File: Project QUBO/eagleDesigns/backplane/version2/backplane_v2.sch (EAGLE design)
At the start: 23 parts, among them U1 TUSB2077ALQFP

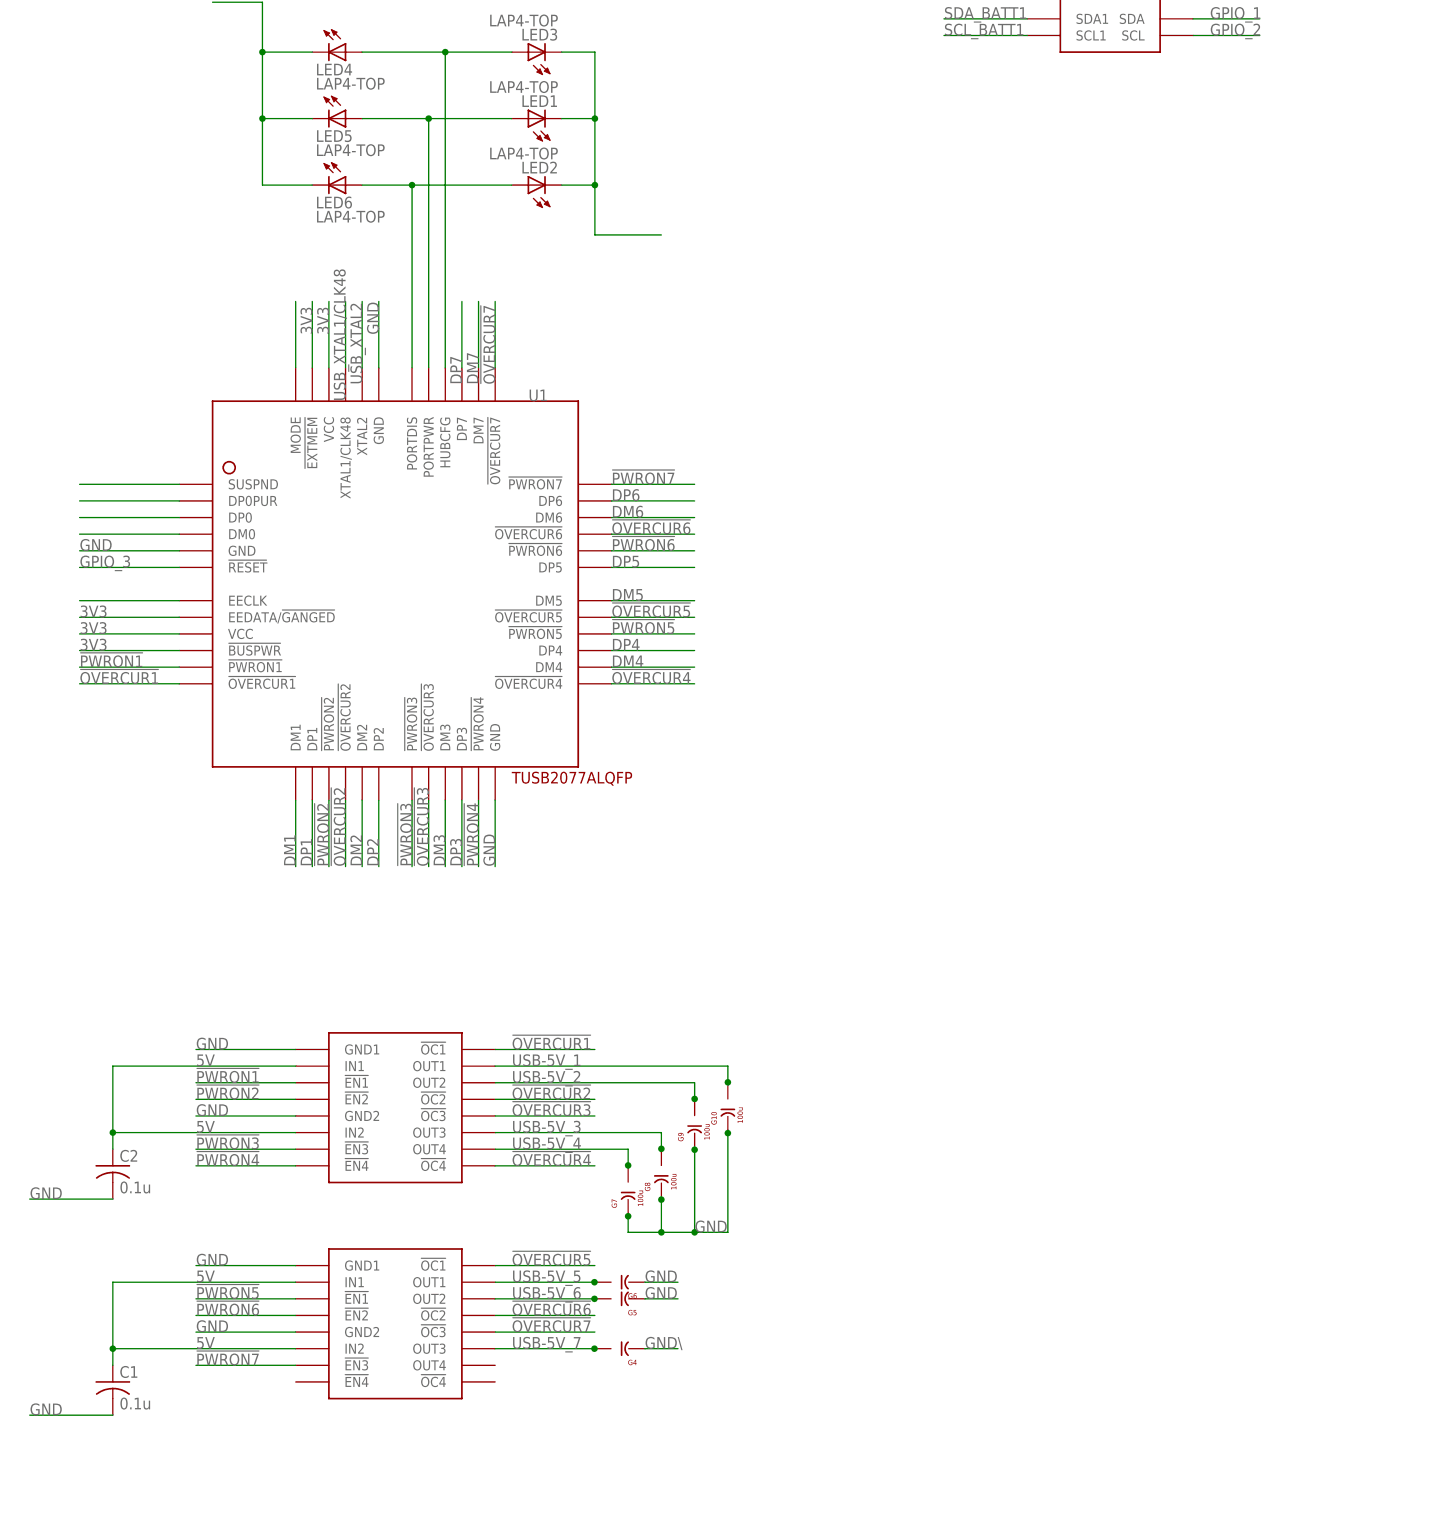
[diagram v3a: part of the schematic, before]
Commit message: 
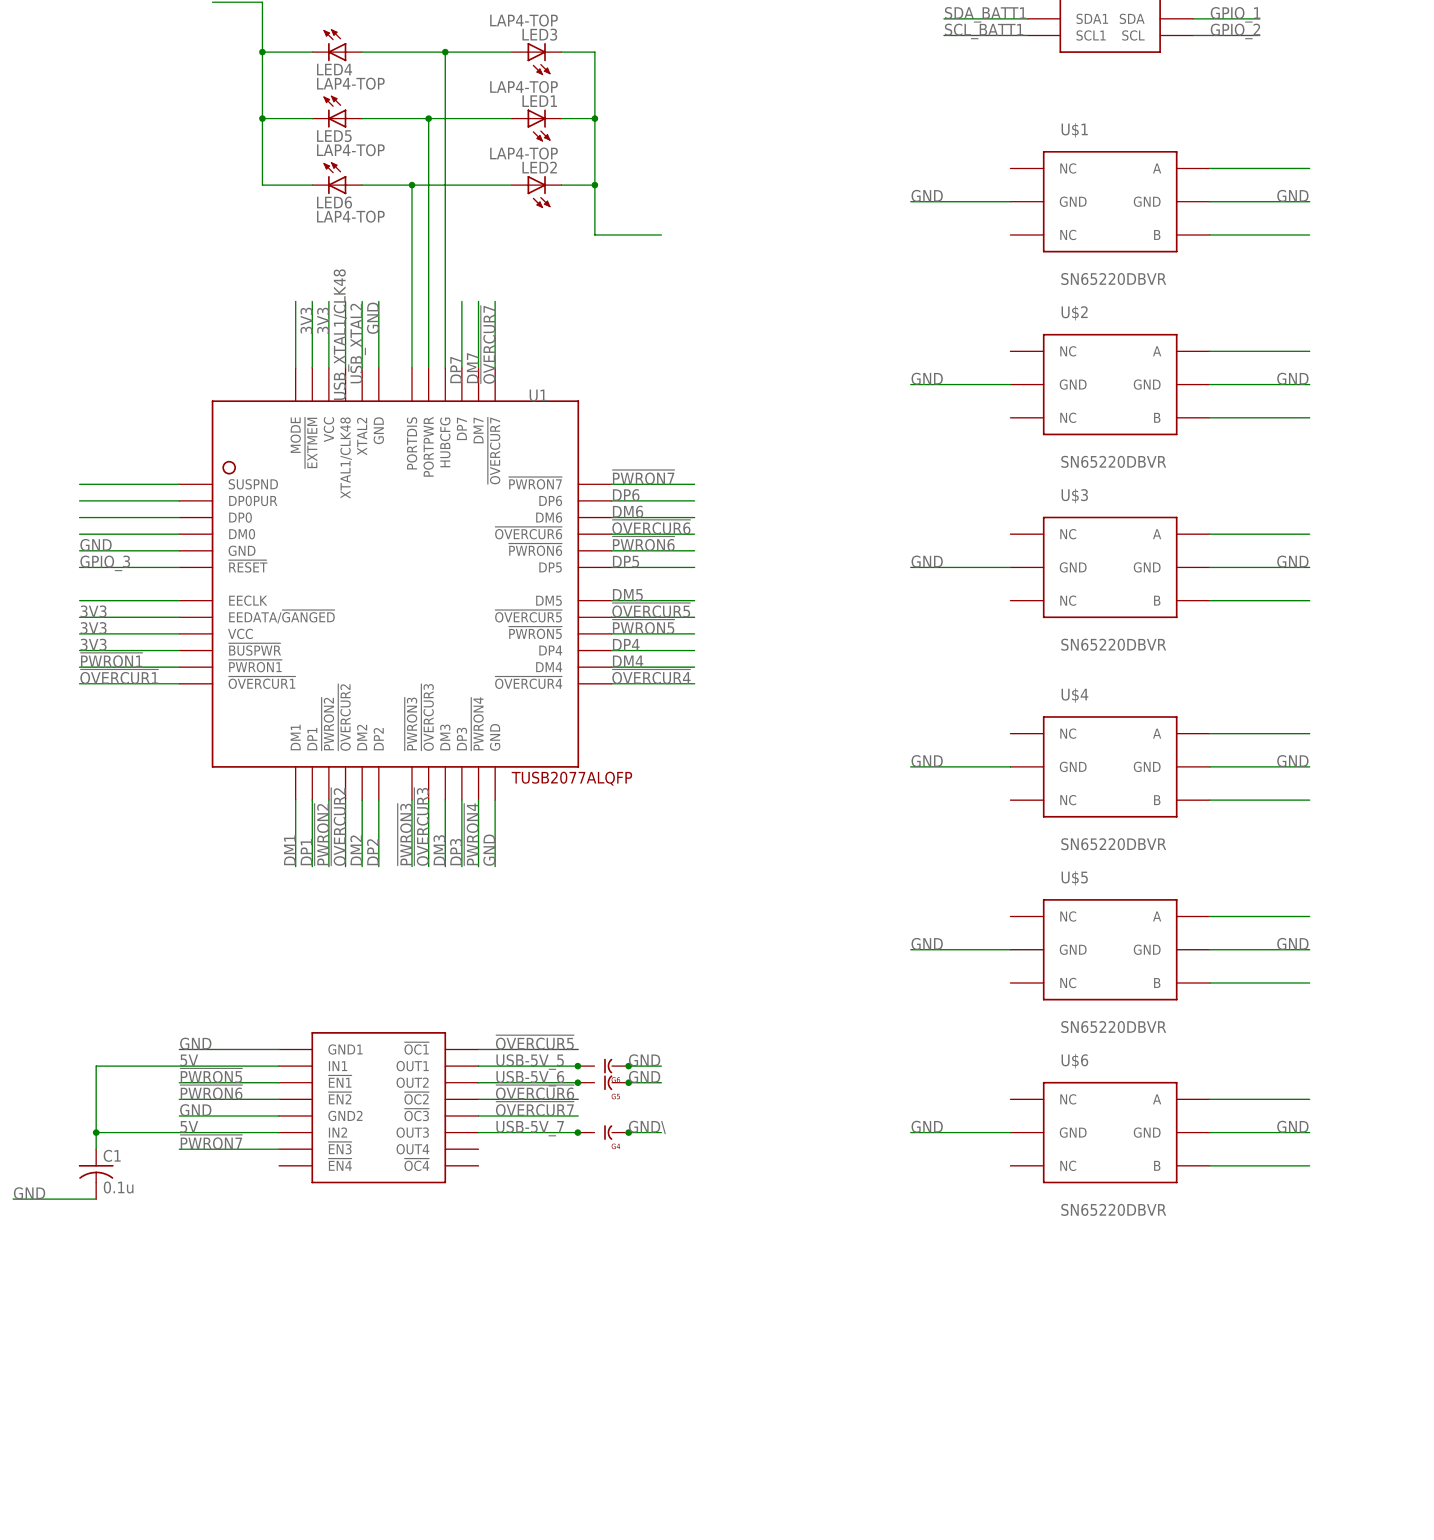
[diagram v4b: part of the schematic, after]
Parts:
- removed C2: 0.1u, resistor:C-USC0603
- removed G10, G7, G8, G9: 100u, avx:F930J107MBA
- removed G2: (no value), texas:TPS2044BBD-SOIC
- added U$1, U$2, U$3, U$4, U$5, U$6: SN65220DBVR, texas:SN65220DBVR
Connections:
- removed net USB-5V_1: G10.+, G2.OUT1
- removed net USB-5V_2: G2.OUT2, G9.+
- removed net USB-5V_3: G2.OUT3, G8.+
- removed net USB-5V_4: G2.OUT4, G7.+
- new net GND\: G4.-
- new net N$10: U$1.B
- new net N$11: U$3.A
- new net N$12: U$3.B
- new net N$13: U$4.A
- new net N$14: U$4.B
- new net N$15: U$5.A
- new net N$16: U$5.B
- new net N$17: U$6.A
- new net N$18: U$6.B
- new net N$6: U$2.A
- new net N$8: U$2.B
- new net N$9: U$1.A
- net !OVERCUR1!: no longer G2.!OC1!
- net !OVERCUR2!: no longer G2.!OC2!
- net !OVERCUR3!: no longer G2.!OC3!
- net !OVERCUR4!: no longer G2.!OC4!
- net !PWRON1!: no longer G2.!EN1!
- net !PWRON2!: no longer G2.!EN2!
- net !PWRON3!: no longer G2.!EN3!
- net !PWRON4!: no longer G2.!EN4!
- net 5V: no longer C2.1, G2.IN1, G2.IN2
- net GND: now also G5.-, G6.-, U$1.GND@2, U$1.GND@5, U$2.GND@2, U$2.GND@5, U$3.GND@2, U$3.GND@5, U$4.GND@2, U$4.GND@5, U$5.GND@2, U$5.GND@5, U$6.GND@2, U$6.GND@5; no longer C2.2, G10.-, G2.GND1, G2.GND2, G7.-, G8.-, G9.-
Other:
- moved on the sheet: C1, G4, G5, G6

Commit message: 
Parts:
- removed G4, G5, G6: (no value), avx:F930J107MBA
- removed JP2, JP3, JP4: MPTC-01-80, samtec:MPTC-01-80
- removed LED1, LED2, LED3, LED4, LED5, LED6: LAP4-TOP, led:LAP4-TOP
- added C2, C3: (no value), resistor:C-USC0805
- added CPU_USB_CPU: (no value), molex:KK254_VERT_2PIN22-29-2021
- added CPU_USB_CPU_TRANS, U$7: SN65220DBVR, texas:SN65220DBVR
- added R1, R2: 27, resistor:R-US_R0805
- added R3: 1.5k, resistor:R-US_R0805
- renumbered G3 to 7USB_PWR, U1 to 7USB
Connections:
- removed net GPIO_10: JP1.P$12, JP2.P$12, JP3.P$12, JP4.P$12
- removed net GPIO_11: JP1.P$13, JP2.P$13, JP3.P$13, JP4.P$13
- removed net GPIO_12: JP1.P$14, JP2.P$14, JP3.P$14, JP4.P$14
- removed net GPIO_13: JP1.P$15, JP2.P$15, JP3.P$15, JP4.P$15
- removed net GPIO_14: JP1.P$16, JP2.P$16, JP3.P$16, JP4.P$16
- removed net GPIO_15: JP1.P$23, JP2.P$23, JP3.P$23, JP4.P$23
- removed net GPIO_16: JP1.P$24, JP2.P$24, JP3.P$24, JP4.P$24
- removed net GPIO_17: JP1.P$25, JP2.P$25, JP3.P$25, JP4.P$25
- removed net GPIO_18: JP1.P$26, JP2.P$26, JP3.P$26, JP4.P$26
- removed net GPIO_19: JP1.P$27, JP2.P$27, JP3.P$27, JP4.P$27
- removed net GPIO_20: JP1.P$28, JP2.P$28, JP3.P$28, JP4.P$28
- removed net GPIO_21: JP1.P$29, JP2.P$29, JP3.P$29, JP4.P$29
- removed net GPIO_22: JP1.P$30, JP2.P$30, JP3.P$30, JP4.P$30
- removed net GPIO_23: JP1.P$31, JP2.P$31, JP3.P$31, JP4.P$31
- removed net GPIO_24: JP1.P$32, JP2.P$32, JP3.P$32, JP4.P$32
- removed net GPIO_25: JP1.P$33, JP2.P$33, JP3.P$33, JP4.P$33
- removed net GPIO_26: JP1.P$34, JP2.P$34, JP3.P$34, JP4.P$34
- removed net GPIO_27: JP1.P$35, JP2.P$35, JP3.P$35, JP4.P$35
- removed net GPIO_28: JP1.P$36, JP2.P$36, JP3.P$36, JP4.P$36
- removed net GPIO_29: JP1.P$43, JP2.P$43, JP3.P$43, JP4.P$43
- removed net GPIO_30: JP1.P$44, JP2.P$44, JP3.P$44, JP4.P$44
- removed net GPIO_31: JP1.P$45, JP2.P$45, JP3.P$45, JP4.P$45
- removed net GPIO_32: JP1.P$46, JP2.P$46, JP3.P$46, JP4.P$46
- removed net GPIO_33: JP1.P$47, JP2.P$47, JP3.P$47, JP4.P$47
- removed net GPIO_34: JP1.P$48, JP2.P$48, JP3.P$48, JP4.P$48
- removed net GPIO_35: JP1.P$49, JP2.P$49, JP3.P$49, JP4.P$49
- removed net GPIO_36: JP1.P$50, JP2.P$50, JP3.P$50, JP4.P$50
- removed net GPIO_37: JP1.P$51, JP2.P$51, JP3.P$51, JP4.P$51
- removed net GPIO_38: JP1.P$52, JP2.P$52, JP3.P$52, JP4.P$52
- removed net GPIO_39: JP1.P$53, JP2.P$53, JP3.P$53, JP4.P$53
- removed net GPIO_40: JP1.P$54, JP2.P$54, JP3.P$54, JP4.P$54
- removed net GPIO_41: JP1.P$55, JP2.P$55, JP3.P$55, JP4.P$55
- removed net GPIO_42: JP1.P$56, JP2.P$56, JP3.P$56, JP4.P$56
- removed net GPIO_43: JP1.P$63, JP2.P$63, JP3.P$63, JP4.P$63
- removed net GPIO_44: JP1.P$64, JP2.P$64, JP3.P$64, JP4.P$64
- removed net GPIO_45: JP1.P$65, JP2.P$65, JP3.P$65, JP4.P$65
- removed net GPIO_46: JP1.P$66, JP2.P$66, JP3.P$66, JP4.P$66
- removed net GPIO_47: JP1.P$67, JP2.P$67, JP3.P$67, JP4.P$67
- removed net GPIO_48: JP1.P$68, JP2.P$68, JP3.P$68, JP4.P$68
- removed net GPIO_49: JP1.P$69, JP2.P$69, JP3.P$69, JP4.P$69
- removed net GPIO_50: JP1.P$70, JP2.P$70, JP3.P$70, JP4.P$70
- removed net GPIO_51: JP1.P$71, JP2.P$71, JP3.P$71, JP4.P$71
- removed net GPIO_52: JP1.P$72, JP2.P$72, JP3.P$72, JP4.P$72
- removed net GPIO_53: JP1.P$73, JP2.P$73, JP3.P$73, JP4.P$73
- removed net GPIO_54: JP1.P$74, JP2.P$74, JP3.P$74, JP4.P$74
- removed net GPIO_55: JP1.P$75, JP2.P$75, JP3.P$75, JP4.P$75
- removed net GPIO_56: JP1.P$76, JP2.P$76, JP3.P$76, JP4.P$76
- removed net GPIO_9: JP1.P$11, JP2.P$11, JP3.P$11, JP4.P$11
- removed net N$3: 7USB.DP0
- removed net N$4: 7USB.DM0
- removed net N$43: 7USB.PORTDIS, LED2.A, LED6.A
- removed net N$44: 7USB.PORTPWR, LED1.A, LED5.A
- removed net N$45: 7USB.HUBCFG, LED3.A, LED4.A
- removed net THR_SCL: JP1.P$1, JP2.P$1, JP3.P$1, JP4.P$1
- removed net THR_SDA: JP1.P$2, JP2.P$2, JP3.P$2, JP4.P$2
- removed net USB-M_1: JP1.P$61
- removed net USB-M_2: JP2.P$61
- removed net USB-M_3: JP3.P$61
- removed net USB-M_4: JP4.P$61
- removed net USB-P_1: JP1.P$41
- removed net USB-P_2: JP2.P$41
- removed net USB-P_3: JP3.P$41
- removed net USB-P_4: JP4.P$41
- new net CANH: JP1.P$25
- new net CANL: JP1.P$26
- new net CE_0: JP1.P$52
- new net CE_1: JP1.P$53
- new net CE_2: JP1.P$54
- new net CE_3: JP1.P$55
- new net CE_4: JP1.P$56
- new net CPU_USB_CPU_D+: 7USB.DP0, C3.1, CPU_USB_CPU_TRANS.A, R1.2, R3.1
- new net CPU_USB_CPU_D-: 7USB.DM0, C2.1, CPU_USB_CPU_TRANS.B, R2.2
- new net CTS_0: JP1.P$47
- new net CTS_1: JP1.P$31
- new net CTS_2: JP1.P$71
- new net CTS_3: JP1.P$75
- new net CTS_4: JP1.P$79
- new net FLEX_USB_1+\: JP1.P$17
- new net FLEX_USB_1-: JP1.P$16
- new net FLEX_USB_2+: JP1.P$14
- new net FLEX_USB_2-: JP1.P$13
- new net GPIO_0: JP1.P$35
- new net MISO: JP1.P$51
- new net MOSI: JP1.P$50
- new net N$19: CPU_USB_CPU.P$1, R2.1
- new net N$20: U$7.A
- new net N$21: U$7.B
- new net PWM_0: JP1.P$7
- new net PWM_1: JP1.P$8
- new net RTS_0: JP1.P$48
- new net RTS_1: JP1.P$32
- new net RTS_2: JP1.P$72
- new net RTS_3: JP1.P$76
- new net RTS_4: JP1.P$80
- new net RX_0: JP1.P$45
- new net RX_1: JP1.P$29
- new net RX_2: JP1.P$69
- new net RX_3: JP1.P$73
- new net RX_4: JP1.P$77
- new net SCL_0: JP1.P$28
- new net SCL_1: JP1.P$10
- new net SCL_2: JP1.P$60
- new net SCL_3: JP1.P$6
- new net SDA_0: JP1.P$27
- new net SDA_1: JP1.P$9
- new net SDA_2: JP1.P$59
- new net SDA_3: JP1.P$5
- new net SPI_CLK: JP1.P$49
- new net TX_0: JP1.P$46
- new net TX_1: JP1.P$30
- new net TX_2: JP1.P$70
- new net TX_3: JP1.P$74
- new net TX_4: JP1.P$78
- new net USB_1+: JP1.P$20
- new net USB_1-: JP1.P$19
- net 12V: now also JP1.P$1, JP1.P$21, JP1.P$41, JP1.P$61; no longer JP1.P$18, JP1.P$38, JP1.P$58, JP1.P$78, JP2.P$18, JP2.P$38, JP2.P$58, JP2.P$78, JP3.P$18, JP3.P$38, JP3.P$58, JP3.P$78, JP4.P$18, JP4.P$38, JP4.P$58, JP4.P$78
- net 3V3: now also JP1.P$23, JP1.P$3, JP1.P$43, JP1.P$63; no longer JP1.P$19, JP1.P$39, JP1.P$59, JP1.P$79, JP2.P$19, JP2.P$39, JP2.P$59, JP2.P$79, JP3.P$19, JP3.P$39, JP3.P$59, JP3.P$79, JP4.P$19, JP4.P$39, JP4.P$59, JP4.P$79
- net 5V: now also JP1.P$2, JP1.P$22, JP1.P$42, JP1.P$62; no longer JP1.P$20, JP1.P$40, JP1.P$60, JP1.P$80, JP2.P$20, JP2.P$40, JP2.P$60, JP2.P$80, JP3.P$20, JP3.P$40, JP3.P$60, JP3.P$80, JP4.P$20, JP4.P$40, JP4.P$60, JP4.P$80
- net GND: now also C2.2, C3.2, CPU_USB_CPU_TRANS.GND@2, CPU_USB_CPU_TRANS.GND@5, JP1.P$12, JP1.P$15, JP1.P$18, JP1.P$24, JP1.P$33, JP1.P$34, JP1.P$36, JP1.P$39, JP1.P$4, JP1.P$44, JP1.P$64, JP1.POWER2, U$7.GND@2, U$7.GND@5; no longer G5.-, G6.-, JP1.P$17, JP1.P$21, JP1.P$22, JP1.P$42, JP1.P$57, JP1.P$62, JP1.P$77, JP2.P$17, JP2.P$21, JP2.P$22, JP2.P$37, JP2.P$42, JP2.P$57, JP2.P$62, JP2.P$77, JP3.P$17, JP3.P$21, JP3.P$22, JP3.P$37, JP3.P$42, JP3.P$57, JP3.P$62, JP3.P$77, JP4.P$17, JP4.P$21, JP4.P$22, JP4.P$37, JP4.P$42, JP4.P$57, JP4.P$62, JP4.P$77, LED1.C, LED2.C, LED3.C
- net GND\: now also JP1.P$40; no longer G4.-
- net GPIO_1: now also JP1.P$38; no longer JP1.P$3, JP2.P$3, JP3.P$3, JP4.P$3
- net GPIO_2: now also JP1.P$11; no longer JP1.P$4, JP2.P$4, JP3.P$4, JP4.P$4
- net GPIO_3: now also JP1.P$57; no longer JP1.P$5, JP2.P$5, JP3.P$5, JP4.P$5
- net GPIO_4: now also JP1.P$58; no longer JP1.P$6, JP2.P$6, JP3.P$6, JP4.P$6
- net GPIO_5: now also JP1.P$65; no longer JP1.P$7, JP2.P$7, JP3.P$7, JP4.P$7
- net GPIO_6: now also JP1.P$66; no longer JP1.P$8, JP2.P$8, JP3.P$8, JP4.P$8
- net GPIO_7: now also JP1.P$67; no longer JP1.P$9, JP2.P$9, JP3.P$9, JP4.P$9
- net GPIO_8: now also JP1.P$68; no longer JP1.P$10, JP2.P$10, JP3.P$10, JP4.P$10
- net N$2: now also R3.2
- net N$5: now also CPU_USB_CPU.P$2, R1.1; no longer LED4.C, LED5.C, LED6.C
- net USB-5V_5: no longer G6.+
- net USB-5V_6: no longer G5.+
- net USB-5V_7: no longer G4.+
- net V_BATT: no longer JP1.POWER2, JP2.POWER1, JP2.POWER2, JP3.POWER1, JP3.POWER2, JP4.POWER1, JP4.POWER2
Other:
- moved on the sheet: JP1

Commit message: 
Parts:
- removed G1: (no value), NXP:PCA9540BTSSOP8
- added 5.0, 5.1, 5.2, 5.3, 5.4, 5.5, 5.6, 5.7: M250_5PIN, molex:M250_5PIN
- added ACT-PWR_IN, ACT-PWR_OUT, SYS-GND_0, SYS-GND_1, SYS-GND_2, SYS-GND_3: SUPERSABRE_2CIRCUIT, molex:SUPERSABRE_2CIRCUIT
- added BATTERY-MUX: PCA9546APW, NXP:PCA9546APW
- added IC1: FT232RQ, ftdichip:FT232RQ
- added JP2, JP3, JP4: MPTC-01-80, samtec:MPTC-01-80
- added SPI_LEDS: KK254_6PIN, molex:KK254_6PIN
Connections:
- removed net CE_0: JP1.P$52
- removed net GPIO_5: JP1.P$65
- removed net GPIO_6: JP1.P$66
- removed net GPIO_7: JP1.P$67
- removed net GPIO_8: JP1.P$68
- removed net SCL_BATT0: G1.SCL0
- removed net SCL_BATT1: G1.SCL1
- removed net SDA_BATT0: G1.SDA0
- removed net SDA_BATT1: G1.SDA1
- new net BATT1_SCL: 5.4.P$4, BATTERY-MUX.SC1
- new net BATT1_SDA: 5.5.P$4, BATTERY-MUX.SD1
- new net BATT2_SCL: 5.4.P$3, BATTERY-MUX.SC2
- new net BATT2_SDA: 5.5.P$3, BATTERY-MUX.SD2
- new net CE_DEBUG-LEDS: JP1.P$52, JP2.P$52, JP3.P$52, JP4.P$52, SPI_LEDS.P$1
- new net CTS_5: 5.2.P$3, JP1.P$67, JP2.P$67, JP3.P$67, JP4.P$67
- new net DVL_HCTS: 5.6.P$4
- new net DVL_HRTS: 5.6.P$3
- new net DVL_HRX: 5.6.P$1
- new net DVL_HTX: 5.6.P$2
- new net DVL_SCTS: 5.7.P$5
- new net DVL_SRTS: 5.5.P$1
- new net DVL_SRX: 5.6.P$5
- new net DVL_STX: 5.4.P$1
- new net RTS_5: 5.2.P$4, JP1.P$68, JP2.P$68, JP3.P$68, JP4.P$68
- new net RX_5: 5.2.P$1, JP1.P$65, JP2.P$65, JP3.P$65, JP4.P$65
- new net SHORE_SCL: 5.4.P$2, BATTERY-MUX.SC0
- new net SHORE_SDA: 5.5.P$2, BATTERY-MUX.SD0
- new net TX_5: 5.2.P$2, JP1.P$66, JP2.P$66, JP3.P$66, JP4.P$66
- new net USB_2+: JP2.P$20
- new net USB_2-: JP2.P$19
- new net USB_3+: JP3.P$20
- new net USB_3-: JP3.P$19
- new net USB_4+: JP4.P$20
- new net USB_4-: JP4.P$19
- new net USB_EXT+: 5.7.P$2
- new net USB_EXT-: 5.7.P$1
- net 12V: now also 5.1.P$2, 5.1.P$3, 5.1.P$4, 5.1.P$5, JP2.P$1, JP2.P$21, JP2.P$41, JP2.P$61, JP3.P$1, JP3.P$21, JP3.P$41, JP3.P$61, JP4.P$1, JP4.P$21, JP4.P$41, JP4.P$61
- net 3V3: now also BATTERY-MUX.VDD, JP2.P$23, JP2.P$3, JP2.P$43, JP2.P$63, JP3.P$23, JP3.P$3, JP3.P$43, JP3.P$63, JP4.P$23, JP4.P$3, JP4.P$43, JP4.P$63
- net 5V: now also 5.0.P$1, 5.1.P$1, 5.7.P$4, BATTERY-MUX.!RESET!, JP2.P$2, JP2.P$22, JP2.P$42, JP2.P$62, JP3.P$2, JP3.P$22, JP3.P$42, JP3.P$62, JP4.P$2, JP4.P$22, JP4.P$42, JP4.P$62, SPI_LEDS.P$6; no longer G1.VDD
- net CANH: now also 5.3.P$3, JP2.P$25, JP3.P$25, JP4.P$25
- net CANL: now also 5.3.P$4, JP2.P$26, JP3.P$26, JP4.P$26
- net CE_1: now also JP2.P$53, JP3.P$53, JP4.P$53
- net CE_2: now also JP2.P$54, JP3.P$54, JP4.P$54
- net CE_3: now also JP2.P$55, JP3.P$55, JP4.P$55
- net CE_4: now also JP2.P$56, JP3.P$56, JP4.P$56
- net CTS_0: now also JP2.P$47, JP3.P$47, JP4.P$47
- net CTS_1: now also JP2.P$31, JP3.P$31, JP4.P$31
- net CTS_2: now also JP2.P$71, JP3.P$71, JP4.P$71
- net CTS_3: now also JP2.P$75, JP3.P$75, JP4.P$75
- net CTS_4: now also JP2.P$79, JP3.P$79, JP4.P$79
- net FLEX_USB_1+\: now also JP2.P$17, JP3.P$17, JP4.P$17
- net FLEX_USB_1-: now also JP2.P$16, JP3.P$16, JP4.P$16
- net FLEX_USB_2+: now also JP2.P$14, JP3.P$14, JP4.P$14
- net FLEX_USB_2-: now also JP2.P$13, JP3.P$13, JP4.P$13
- net GND: now also 5.0.P$2, 5.0.P$3, 5.0.P$4, 5.0.P$5, 5.2.P$5, 5.3.P$5, 5.7.P$3, BATTERY-MUX.A0, BATTERY-MUX.A1, BATTERY-MUX.A2, BATTERY-MUX.VSS, JP2.P$12, JP2.P$15, JP2.P$18, JP2.P$24, JP2.P$33, JP2.P$34, JP2.P$36, JP2.P$37, JP2.P$39, JP2.P$4, JP2.P$44, JP2.P$64, JP2.POWER2, JP3.P$12, JP3.P$15, JP3.P$18, JP3.P$24, JP3.P$33, JP3.P$34, JP3.P$36, JP3.P$37, JP3.P$39, JP3.P$4, JP3.P$44, JP3.P$64, JP3.POWER2, JP4.P$12, JP4.P$15, JP4.P$18, JP4.P$24, JP4.P$33, JP4.P$34, JP4.P$36, JP4.P$37, JP4.P$39, JP4.P$4, JP4.P$44, JP4.P$64, JP4.POWER2, SPI_LEDS.P$5, SYS-GND_0.P$1, SYS-GND_0.P$2, SYS-GND_1.P$1, SYS-GND_1.P$2, SYS-GND_2.P$1, SYS-GND_2.P$2, SYS-GND_3.P$1, SYS-GND_3.P$2; no longer G1.GND
- net GND\: now also JP2.P$40, JP3.P$40, JP4.P$40
- net GPIO_0: now also JP2.P$35, JP3.P$35, JP4.P$35
- net GPIO_1: now also JP2.P$38, JP3.P$38, JP4.P$38; no longer G1.SDA
- net GPIO_2: now also JP2.P$11, JP3.P$11, JP4.P$11; no longer G1.SCL
- net GPIO_3: now also JP2.P$57, JP3.P$57, JP4.P$57
- net GPIO_4: now also JP2.P$58, JP3.P$58, JP4.P$58
- net MISO: now also JP2.P$51, JP3.P$51, JP4.P$51, SPI_LEDS.P$2
- net MOSI: now also JP2.P$50, JP3.P$50, JP4.P$50, SPI_LEDS.P$3
- net PWM_0: now also JP2.P$7, JP3.P$7, JP4.P$7
- net PWM_1: now also JP2.P$8, JP3.P$8, JP4.P$8
- net RTS_0: now also JP2.P$48, JP3.P$48, JP4.P$48
- net RTS_1: now also JP2.P$32, JP3.P$32, JP4.P$32
- net RTS_2: now also JP2.P$72, JP3.P$72, JP4.P$72
- net RTS_3: now also JP2.P$76, JP3.P$76, JP4.P$76
- net RTS_4: now also JP2.P$80, JP3.P$80, JP4.P$80
- net RX_0: now also JP2.P$45, JP3.P$45, JP4.P$45
- net RX_1: now also JP2.P$29, JP3.P$29, JP4.P$29
- net RX_2: now also JP2.P$69, JP3.P$69, JP4.P$69
- net RX_3: now also JP2.P$73, JP3.P$73, JP4.P$73
- net RX_4: now also JP2.P$77, JP3.P$77, JP4.P$77
- net SCL_0: now also BATTERY-MUX.SCL, JP2.P$28, JP3.P$28, JP4.P$28
- net SCL_1: now also JP2.P$10, JP3.P$10, JP4.P$10
- net SCL_2: now also 5.4.P$5, JP2.P$60, JP3.P$60, JP4.P$60
- net SCL_3: now also 5.3.P$2, JP2.P$6, JP3.P$6, JP4.P$6
- net SDA_0: now also BATTERY-MUX.SDA, JP2.P$27, JP3.P$27, JP4.P$27
- net SDA_1: now also JP2.P$9, JP3.P$9, JP4.P$9
- net SDA_2: now also 5.5.P$5, JP2.P$59, JP3.P$59, JP4.P$59
- net SDA_3: now also 5.3.P$1, JP2.P$5, JP3.P$5, JP4.P$5
- net SPI_CLK: now also JP2.P$49, JP3.P$49, JP4.P$49, SPI_LEDS.P$4
- net TX_0: now also JP2.P$46, JP3.P$46, JP4.P$46
- net TX_1: now also JP2.P$30, JP3.P$30, JP4.P$30
- net TX_2: now also JP2.P$70, JP3.P$70, JP4.P$70
- net TX_3: now also JP2.P$74, JP3.P$74, JP4.P$74
- net TX_4: now also JP2.P$78, JP3.P$78, JP4.P$78
- net V_BATT: now also JP2.POWER1, JP3.POWER1, JP4.POWER1
